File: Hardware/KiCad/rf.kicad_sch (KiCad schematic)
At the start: 29 parts, among them J8 Conn_Coaxial, U4 CC1200, Y3 40 MHz

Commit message: rough layout of cc1200
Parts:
- added C11, C121, C131, C151, C221, C251, C271, C281, C51: (no value), symbol pkl_device:pkl_C_Small
- C171: renamed from C52; value 10n -> (none); footprint Capacitor_SMD:C_0402_1005Metric -> (none)
- C172: renamed from C55; value 100p -> (none); footprint Capacitor_SMD:C_0402_1005Metric -> (none)
- C173: renamed from C50; value 56p -> (none); footprint Capacitor_SMD:C_0402_1005Metric -> (none)
- C174: renamed from C49; value 39p -> (none); footprint Capacitor_SMD:C_0402_1005Metric -> (none)
- C175: renamed from C54; value 6.2p -> (none); footprint Capacitor_SMD:C_0402_1005Metric -> (none)
- C176: renamed from C51; value 2.2p -> (none); footprint Capacitor_SMD:C_0402_1005Metric -> (none)
- C181: renamed from C53; value 5.1p -> (none); footprint Capacitor_SMD:C_0402_1005Metric -> (none)
- C191: renamed from C47; value 5.1p -> (none); footprint Capacitor_SMD:C_0402_1005Metric -> (none)
- C201: renamed from C48; value 5.1p -> (none); footprint Capacitor_SMD:C_0402_1005Metric -> (none)
- C211: renamed from C13; value 10n -> (none); footprint Capacitor_SMD:C_0402_1005Metric -> (none)
- C231: renamed from C10; value 1.5n -> (none); footprint Capacitor_SMD:C_0402_1005Metric -> (none)
- C261: renamed from C12; value 47n -> (none); footprint Capacitor_SMD:C_0402_1005Metric -> (none)
- C291: renamed from C11; value 47n -> (none); footprint Capacitor_SMD:C_0402_1005Metric -> (none)
- C301: renamed from C8; value 12p -> (none); footprint Capacitor_SMD:C_0402_1005Metric -> (none)
- C311: renamed from C9; value 12p -> (none); footprint Capacitor_SMD:C_0402_1005Metric -> (none)
- C61: renamed from C14; value 220n -> (none); footprint Capacitor_SMD:C_0402_1005Metric -> (none)
- L171: renamed from L6; value 56n -> (none); footprint Inductor_SMD:L_0402_1005Metric -> (none)
- L172: renamed from L7; value 15n -> (none); footprint Inductor_SMD:L_0402_1005Metric -> (none)
- L173: renamed from L8; value 43n -> (none); footprint Inductor_SMD:L_0402_1005Metric -> (none)
- L174: renamed from L9; value 22n -> (none); footprint Inductor_SMD:L_0402_1005Metric -> (none)
- L191: renamed from L3; value 56n -> (none); footprint Inductor_SMD:L_0402_1005Metric -> (none)
- L192: renamed from L2; value 27n -> (none); footprint Inductor_SMD:L_0402_1005Metric -> (none)
- L193: renamed from L5; value 15n -> (none); footprint Inductor_SMD:L_0402_1005Metric -> (none)
- L201: renamed from L4; value 27n -> (none); footprint Inductor_SMD:L_0402_1005Metric -> (none)
- R141: renamed from R9; value 56k -> (none); footprint Resistor_SMD:R_0402_1005Metric -> (none)
- R171: renamed from R29; value 18 -> (none); footprint Resistor_SMD:R_0402_1005Metric -> (none)
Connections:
- net GND: now also C11.2, C121.2, C131.2, C151.2, C221.2, C251.2, C271.2, C281.2, C51.2
- net PA: now also L171.1; no longer L171.2
- net VDD: now also C11.1, C121.1, C131.1, C151.1, C221.1, C251.1, C271.1, C281.1, C51.1
- net at C173.2, R171.2: now also L171.2; no longer L171.1
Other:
- note added: "CC1200 decoupling"
- moved on the sheet: C171, C172, C173, L171, R171

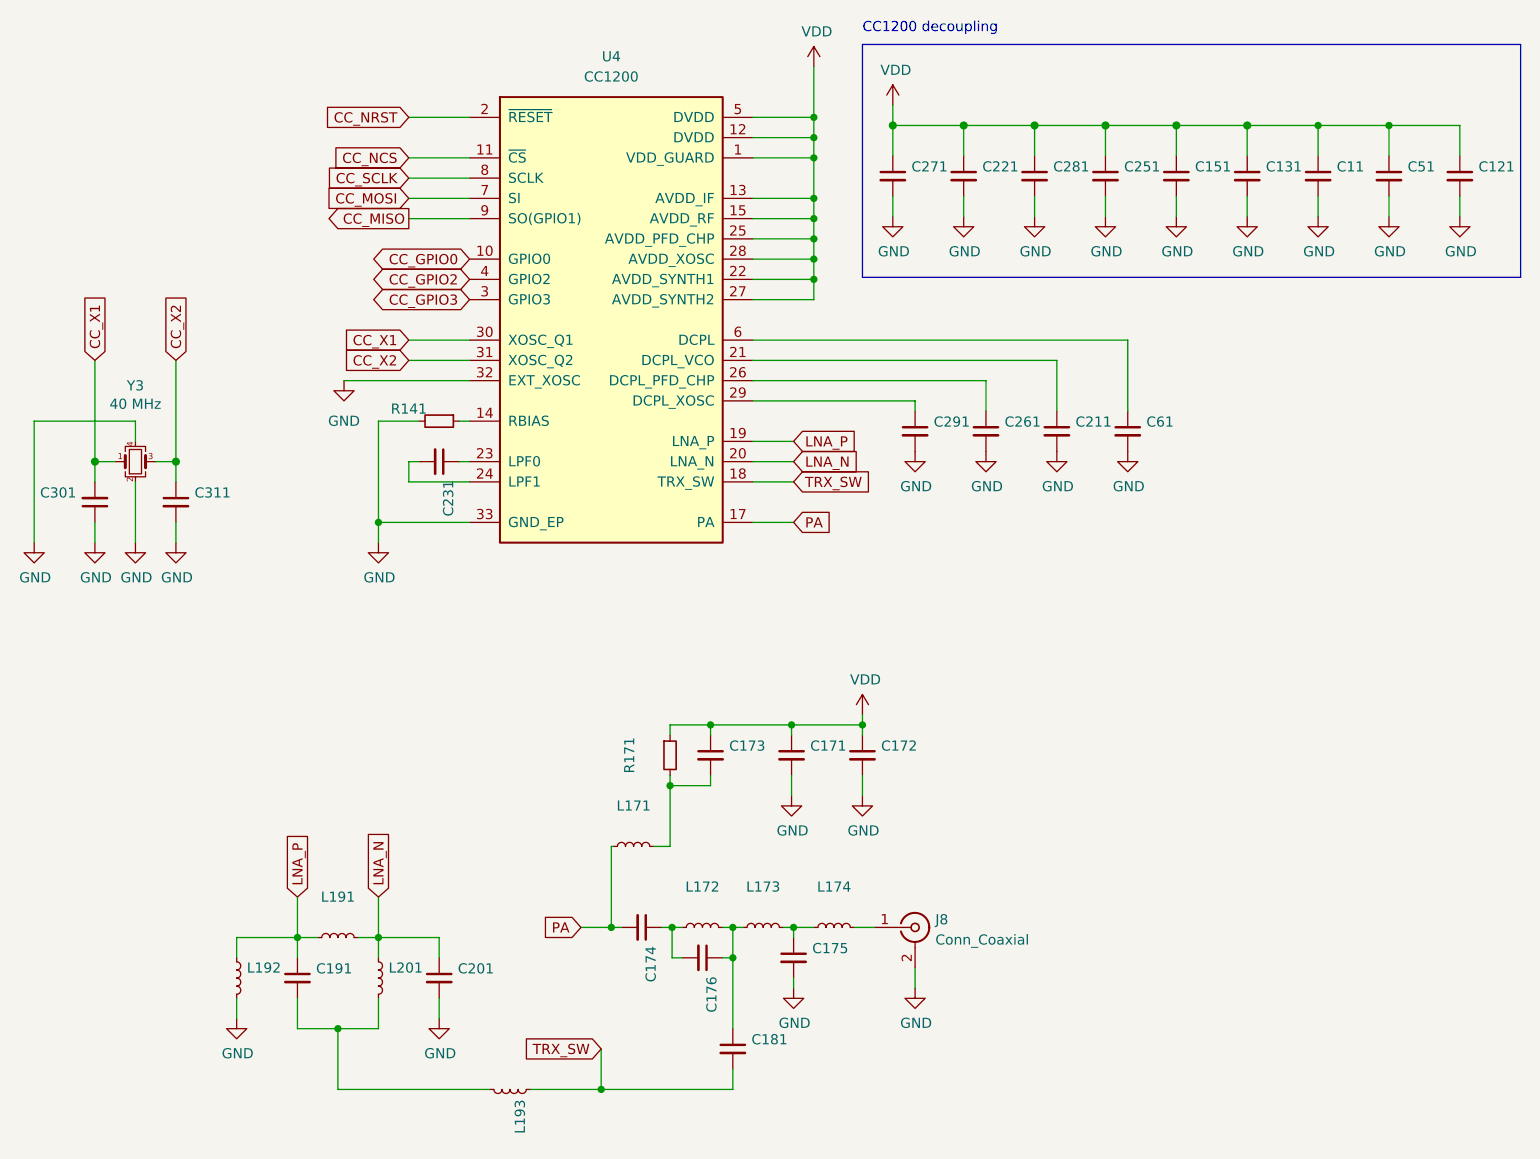
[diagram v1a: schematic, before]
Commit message: fix issue 21 & 20 & move MCU to align w/ grid
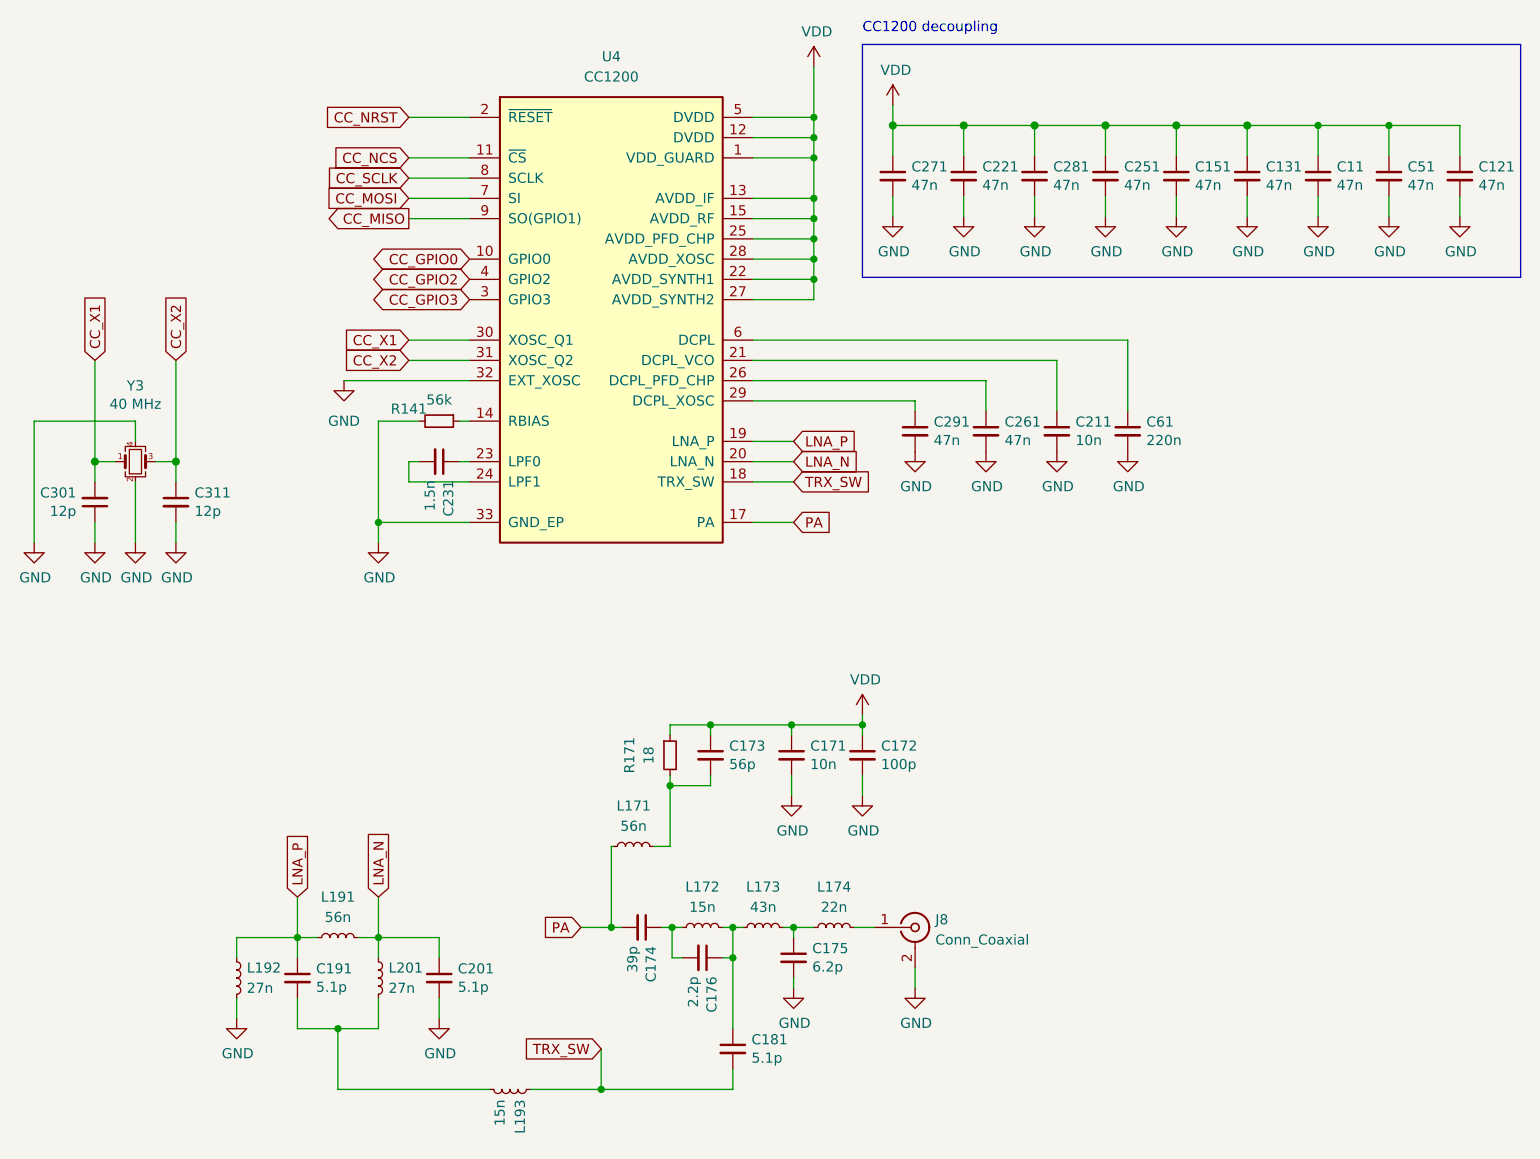
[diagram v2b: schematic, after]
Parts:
- C11, C121, C131, C151, C221, C251, C261, C271, C281, C291, C51: value (none) -> 47n; footprint (none) -> Capacitor_SMD:C_0402_1005Metric
- C171, C211: value (none) -> 10n; footprint (none) -> Capacitor_SMD:C_0402_1005Metric
- C172: value (none) -> 100p; footprint (none) -> Capacitor_SMD:C_0402_1005Metric
- C173: value (none) -> 56p; footprint (none) -> Capacitor_SMD:C_0402_1005Metric
- C174: value (none) -> 39p; footprint (none) -> Capacitor_SMD:C_0402_1005Metric
- C175: value (none) -> 6.2p; footprint (none) -> Capacitor_SMD:C_0402_1005Metric
- C176: value (none) -> 2.2p; footprint (none) -> Capacitor_SMD:C_0402_1005Metric
- C181, C191, C201: value (none) -> 5.1p; footprint (none) -> Capacitor_SMD:C_0402_1005Metric
- C231: value (none) -> 1.5n; footprint (none) -> Capacitor_SMD:C_0402_1005Metric
- C301, C311: value (none) -> 12p; footprint (none) -> Capacitor_SMD:C_0402_1005Metric
- C61: value (none) -> 220n; footprint (none) -> Capacitor_SMD:C_0402_1005Metric
- L171, L191: value (none) -> 56n; footprint (none) -> Inductor_SMD:L_0402_1005Metric
- L172, L193: value (none) -> 15n; footprint (none) -> Inductor_SMD:L_0402_1005Metric
- L173: value (none) -> 43n; footprint (none) -> Inductor_SMD:L_0402_1005Metric
- L174: value (none) -> 22n; footprint (none) -> Inductor_SMD:L_0402_1005Metric
- L192, L201: value (none) -> 27n; footprint (none) -> Inductor_SMD:L_0402_1005Metric
- R141: value (none) -> 56k; footprint (none) -> Resistor_SMD:R_0402_1005Metric
- R171: value (none) -> 18; footprint (none) -> Resistor_SMD:R_0402_1005Metric
